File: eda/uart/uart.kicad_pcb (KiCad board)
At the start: 2 copper layers, 133.3 x 85.2 mm, 52 parts, among them J1 UART, J2 Bus expansion, U1 74HCT08, U10 74HCT574, U11 74HCT595, U12 74HCT595, U13 CD74HCT40105E, U14 CD74HCT40105E, U15 74HCT00, U16 74HCT74, U17 74HCT193, U18 74HCT32, U2 74HCT14, U3 74HCT193, U4 74HCT193, U5 74HCT165, U6 74HCT165, U7 74HCT139, U8 CD74HCT40105E, U9 CD74HCT40105E, X1 1.8xx

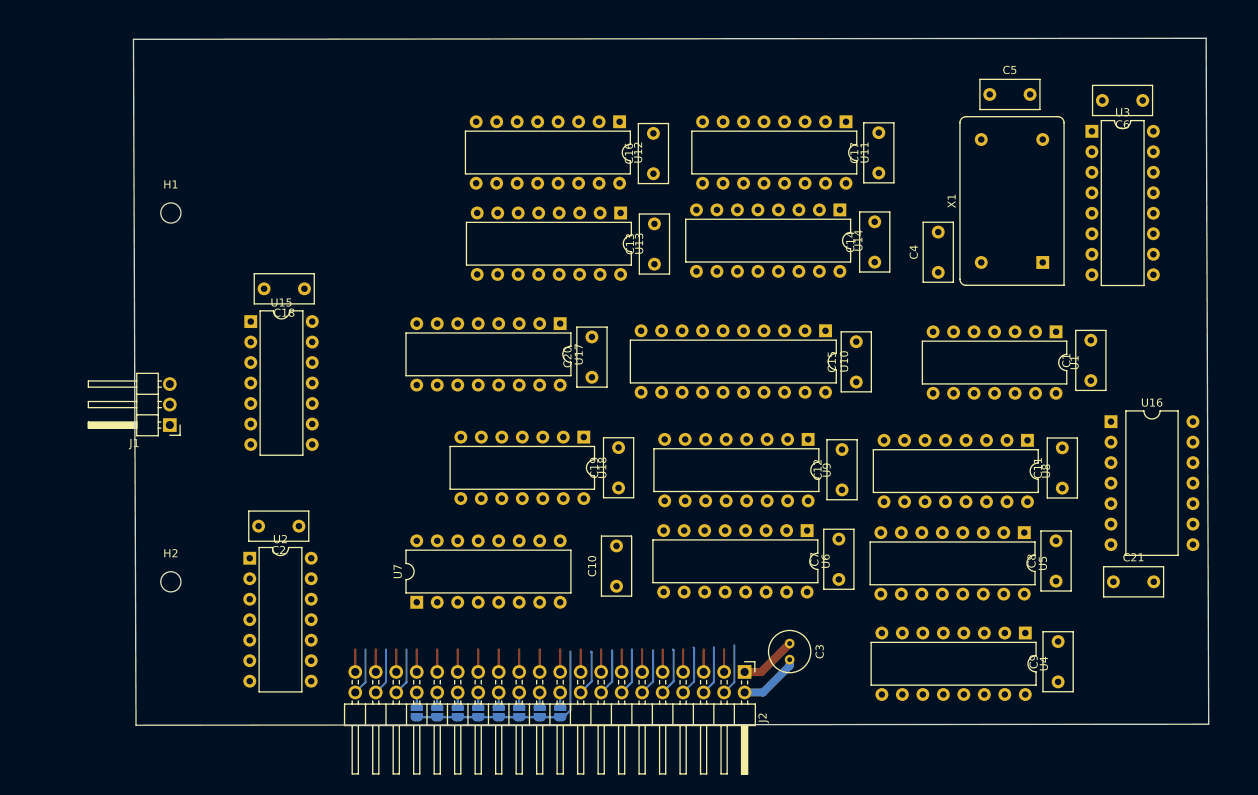
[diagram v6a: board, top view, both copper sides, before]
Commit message: Prelimary UART routing
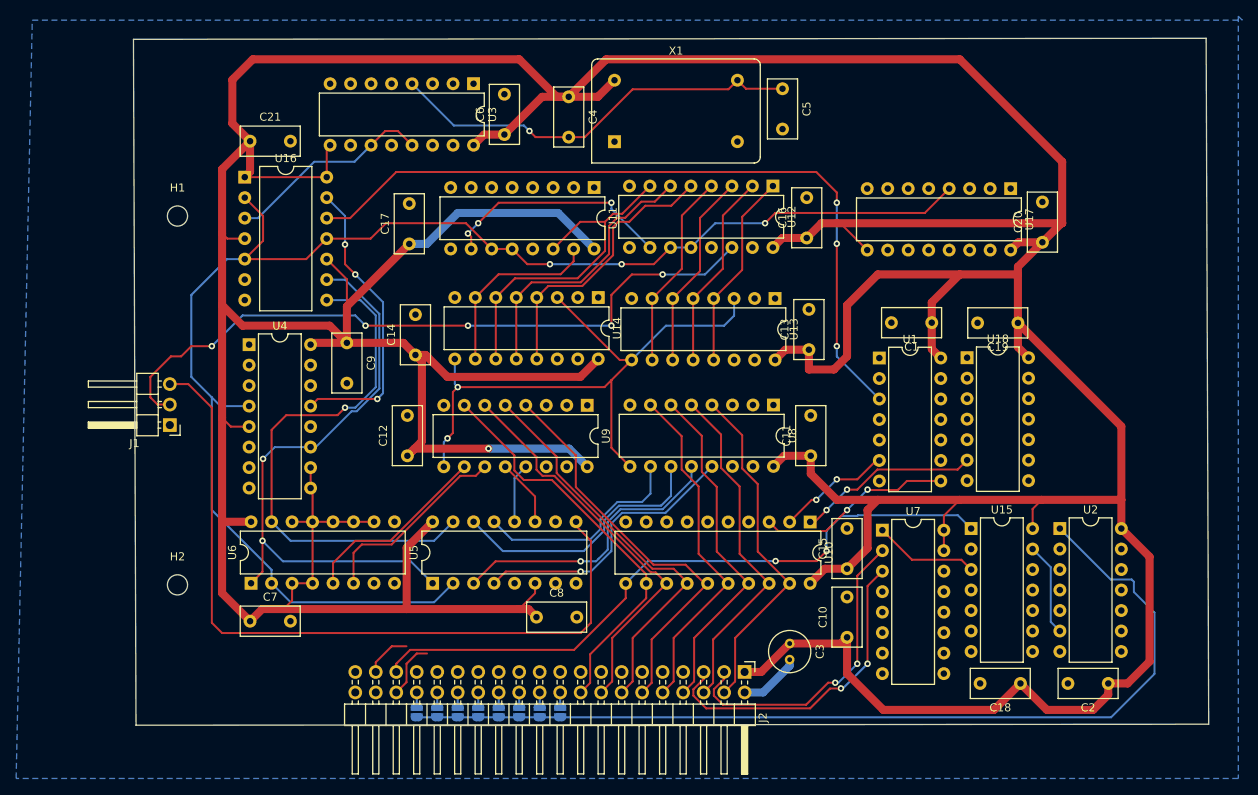
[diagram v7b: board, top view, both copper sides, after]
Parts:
- moved C21 120.2 mm to (53.0, 80.0)
- moved U16 111.6 mm to (52.3, 84.5)
- moved U4 102.6 mm to (52.9, 105.2), turned to 0 degrees
- moved C2 102.2 mm to (159.4, 147.2)
- moved C18 101.3 mm to (148.5, 147.2)
- moved U2 100.5 mm to (153.4, 128.0)
- moved C9 97.7 mm to (65.0, 105.0), turned to -90 degrees
- moved U15 92.9 mm to (142.4, 128.0)
- moved C6 79.2 mm to (84.5, 79.2), turned to 90 degrees
- moved U3 76.9 mm to (80.7, 72.9), turned to -90 degrees
- moved U5 73.6 mm to (75.6, 134.8), turned to 90 degrees
- moved C7 73.2 mm to (53.0, 139.5), turned to 0 degrees
- moved U6 69.2 mm to (53.1, 134.8), turned to 90 degrees
- moved C8 64.6 mm to (88.5, 139.0), turned to 0 degrees
- moved C17 58.9 mm to (72.7, 92.7)
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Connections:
- U15 pad 1: Net-(U15-Pad1) -> /Expansion header/Clock
- U15 pad 2: /Expansion header/Clock -> Net-(U15-Pad2)
- U15 pad 4: (no net) -> GND
- U15 pad 5: (no net) -> GND
- U15 pad 6: (no net) -> unconnected-(U15-Pad6)
- U18 pad 10: unconnected-(U18-Pad10) -> GND
- U18 pad 12: unconnected-(U18-Pad12) -> GND
- U18 pad 13: unconnected-(U18-Pad13) -> GND
- U18 pad 9: unconnected-(U18-Pad9) -> GND
- U2 pad 12: (no net) -> unconnected-(U2-Pad12)
- U2 pad 13: (no net) -> GND
- U2 pad 2: Net-(U15-Pad1) -> Net-(U15-Pad2)
- U2 pad 3: (no net) -> GND
- U2 pad 4: (no net) -> unconnected-(U2-Pad4)
- U7 pad 13: unconnected-(U7B-A1-Pad13) -> GND
- U7 pad 14: unconnected-(U7B-A0-Pad14) -> GND
- U7 pad 15: unconnected-(U7B-E-Pad15) -> VCC
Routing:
- net VCC: track 7.05 -> 774.1 mm, vias 0 -> 1
- net /clock/UartClock: track 0.00 -> 182.5 mm, vias 0 -> 3
- net /transmit/FIFO Transmit/DOR: track 0.00 -> 94.4 mm, vias 0 -> 3
- net /transmit/TX: track 0.00 -> 94.4 mm
- net /Expansion header/~{CS}: track 26.7 -> 118.1 mm
- net /recieve/Reset: track 0.00 -> 89.9 mm, vias 0 -> 2
- net /recieve/RX: track 0.00 -> 87.3 mm, vias 0 -> 5
- net /Expansion header/Clock: track 2.79 -> 83.1 mm, vias 0 -> 2
- net /transmit/~{LatchShiftRegisters}: track 0.00 -> 74.9 mm, vias 0 -> 2
- net /transmit/~{ClockEnable}: track 0.00 -> 66.7 mm, vias 0 -> 1
- net Net-(U3-DOWN): track 0.00 -> 52.0 mm, vias 0 -> 1
- net /Expansion header/D4: track 5.80 -> 50.9 mm
- net /Expansion header/D7: track 5.68 -> 50.3 mm
- net /Expansion header/D5: track 5.86 -> 49.8 mm
- net /Expansion header/D6: track 5.80 -> 49.5 mm
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- added copper zone on B.Cu, net GND

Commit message: Sync
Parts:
- added D1: 1N4001, Diode_THT:D_DO-41_SOD81_P10.16mm_Horizontal, F.Cu at (179.3, 80.0)
- added R1: 10K, Resistor_THT:R_Axial_DIN0207_L6.3mm_D2.5mm_P7.62mm_Horizontal, F.Cu at (179.0, 84.2)
- J2: value Bus expansion -> Conn_02x25_Odd_Even; footprint Connector_PinHeader_2.54mm:PinHeader_2x20_P2.54mm_Horizontal -> Connector_PinHeader_2.54mm:PinHeader_2x25_P2.54mm_Horizontal
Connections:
- J2 pad 11: /Expansion header/A4 -> /Expansion header/A3
- J2 pad 13: /Expansion header/A5 -> /Expansion header/A4
- J2 pad 15: /Expansion header/A6 -> /Expansion header/A5
- J2 pad 17: /Expansion header/A7 -> /Expansion header/A6
- J2 pad 19: /Expansion header/A8 -> /Expansion header/A7
- J2 pad 20: Net-(J2-Pin_20) -> GND
- J2 pad 21: /Expansion header/A9 -> /Expansion header/A8
- J2 pad 23: /Expansion header/A10 -> /Expansion header/A9
- J2 pad 25: /Expansion header/A11 -> /Expansion header/A10
- J2 pad 27: /Expansion header/A12 -> /Expansion header/A11
- J2 pad 29: /Expansion header/A13 -> /Expansion header/A12
- J2 pad 3: /Expansion header/A0 -> GND
- J2 pad 31: /Expansion header/A14 -> /Expansion header/A13
- J2 pad 33: /Expansion header/A15 -> /Expansion header/A14
- J2 pad 35: /Expansion header/Clock -> /Expansion header/A15
- J2 pad 36: /Expansion header/~{RST} -> Net-(J2-Pin_36)
- J2 pad 37: /Expansion header/R~{W} -> GND
- J2 pad 38: /Expansion header/~{NMI} -> GND
- J2 pad 39: /Expansion header/~{DMA} -> /Expansion header/Clock
- J2 pad 40: /Expansion header/~{IRQ} -> /Expansion header/~{RST}
- J2 pad 5: /Expansion header/A1 -> /Expansion header/A0
- J2 pad 7: /Expansion header/A2 -> /Expansion header/A1
- J2 pad 9: /Expansion header/A3 -> /Expansion header/A2
- JP1 pad 1: Net-(J2-Pin_20) -> Net-(J2-Pin_22)
- JP2 pad 1: Net-(J2-Pin_22) -> Net-(J2-Pin_24)
- JP3 pad 1: Net-(J2-Pin_24) -> Net-(J2-Pin_26)
- JP4 pad 1: Net-(J2-Pin_26) -> Net-(J2-Pin_28)
- JP5 pad 1: Net-(J2-Pin_28) -> Net-(J2-Pin_30)
- JP6 pad 1: Net-(J2-Pin_30) -> Net-(J2-Pin_32)
- JP7 pad 1: Net-(J2-Pin_32) -> Net-(J2-Pin_34)
- JP8 pad 1: Net-(J2-Pin_34) -> Net-(J2-Pin_36)
- U11 pad 14: /recieve/FIFO Recieve/D6 -> /Expansion header/D6
- U11 pad 15: /recieve/FIFO Recieve/D7 -> /Expansion header/D7
- U12 pad 1: /recieve/FIFO Recieve/D0 -> /Expansion header/D0
- U12 pad 2: /recieve/FIFO Recieve/D1 -> /Expansion header/D1
- U12 pad 3: /recieve/FIFO Recieve/D2 -> /Expansion header/D2
- U12 pad 4: /recieve/FIFO Recieve/D3 -> /Expansion header/D3
- U12 pad 5: /recieve/FIFO Recieve/D4 -> /Expansion header/D4
- U12 pad 6: /recieve/FIFO Recieve/D5 -> /Expansion header/D5
- U12 pad 7: /recieve/FIFO Recieve/D6 -> /Expansion header/D6
- U13 pad 10: /recieve/FIFO Recieve/D3 -> /Expansion header/D3
- U13 pad 11: /recieve/FIFO Recieve/D2 -> /Expansion header/D2
- U13 pad 12: /recieve/FIFO Recieve/D1 -> /Expansion header/D1
- U13 pad 13: /recieve/FIFO Recieve/D0 -> /Expansion header/D0
- U13 pad 3: /recieve/Reset -> /recieve/FIFO Recieve/SI
- U14 pad 10: /recieve/FIFO Recieve/D7 -> /Expansion header/D7
- U14 pad 11: /recieve/FIFO Recieve/D6 -> /Expansion header/D6
- U14 pad 12: /recieve/FIFO Recieve/D5 -> /Expansion header/D5
- U14 pad 13: /recieve/FIFO Recieve/D4 -> /Expansion header/D4
- U14 pad 3: /recieve/Reset -> /recieve/FIFO Recieve/SI
- U15 pad 10: Net-(U11-~{SRCLR}) -> Net-(U15-Pad10)
- U15 pad 11: Net-(U11-~{SRCLR}) -> Net-(U15-Pad10)
- U15 pad 12: Net-(U17-~{LOAD}) -> Net-(U11-~{SRCLR})
- U15 pad 13: /recieve/Reset -> Net-(D1-A)
- U15 pad 8: Net-(U17-~{LOAD}) -> Net-(U11-~{SRCLR})
- U16 pad 1: VCC -> Net-(U16A-~{R})
- U16 pad 11: /clock/UartClock -> Net-(U16B-C)
- U16 pad 12: /transmit/FIFO Transmit/DOR -> Net-(U16B-D)
- U16 pad 13: Net-(U16B-~{R}) -> VCC
- U16 pad 2: /clock/UartClock -> /transmit/FIFO Transmit/DOR
- U16 pad 3: Net-(U16A-C) -> /clock/UartClock
- U16 pad 5: /clock/UartClock -> /transmit/~{LatchShiftRegisters}
- U16 pad 6: unconnected-(U16A-~{Q}-Pad6) -> /transmit/~{ClockEnable}
- U16 pad 8: /transmit/~{ClockEnable} -> Net-(U16B-D)
- U16 pad 9: /transmit/~{LatchShiftRegisters} -> /clock/UartClock
- U17 pad 11: Net-(U17-~{LOAD}) -> Net-(U11-~{SRCLR})
- U17 pad 13: /recieve/Reset -> Net-(D1-A)
- U2 pad 3: GND -> Net-(D1-A)
- U2 pad 4: unconnected-(U2-Pad4) -> /recieve/FIFO Recieve/SI
- U3 pad 11: Net-(U16A-C) -> Net-(U16B-C)
- U3 pad 13: Net-(U16A-C) -> Net-(U16B-C)
- U4 pad 13: Net-(U16B-~{R}) -> Net-(U16A-~{R})
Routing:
- net Net-(U16B-~{R}): track 36.8 -> 0.00 mm, vias 3 -> 0
- net VCC: track 774.1 -> 810.9 mm, vias 1 -> 4
- net /clock/UartClock: track 182.5 -> 208.4 mm
- net Net-(U16A-C): track 25.9 -> 0.00 mm
- net Net-(J2-Pin_36): track 0.00 -> 7.15 mm
- net /Expansion header/~{RST}: track 7.15 -> 0.00 mm
- net /Expansion header/D7: track 50.3 -> 56.6 mm
- net /Expansion header/D6: track 49.5 -> 55.8 mm
- net /Expansion header/D5: track 49.8 -> 56.2 mm
- net /Expansion header/D4: track 50.9 -> 57.2 mm
- net GND: track 7.72 -> 13.6 mm
- net /Expansion header/R~{W}: track 5.83 -> 0.00 mm
- net /Expansion header/D3: track 43.0 -> 48.7 mm
- net /Expansion header/D2: track 43.0 -> 48.7 mm
- net /Expansion header/D1: track 43.0 -> 48.7 mm
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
